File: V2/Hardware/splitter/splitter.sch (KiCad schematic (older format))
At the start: 21 parts, among them J0 Rpi_40Pin_F, J1 Control_seg:1, J2 Control_seg:2, J3 Control_seg:3, J4 Molex_PSU_F, J5 Siren, J6 USB_A_F, K0 RELRAS0515, Q1 BD139-16

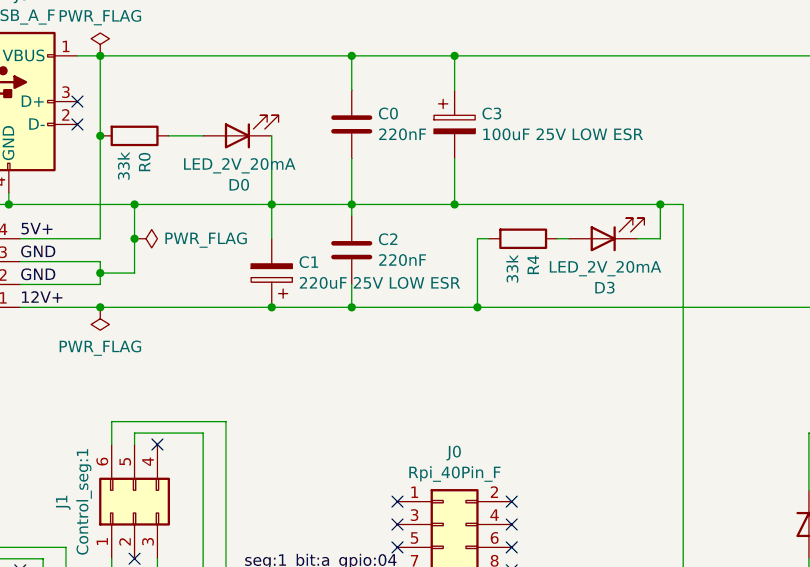
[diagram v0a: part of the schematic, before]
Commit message: update capacitors
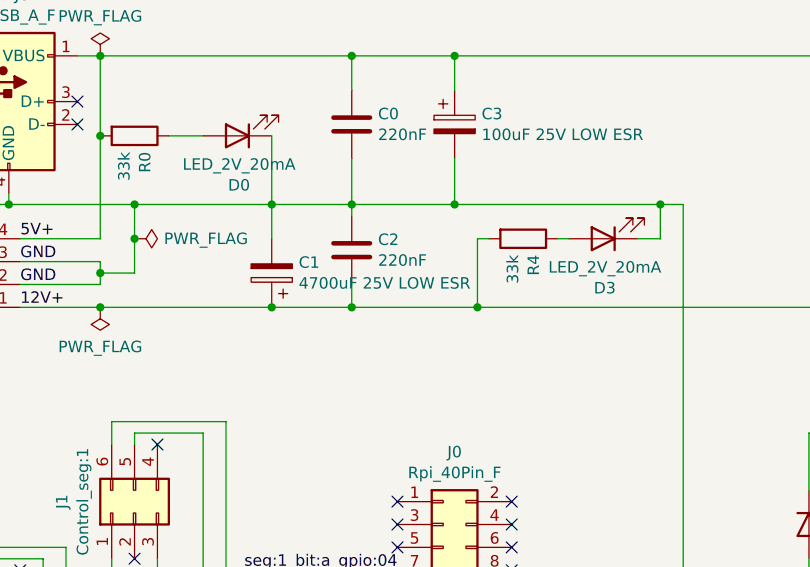
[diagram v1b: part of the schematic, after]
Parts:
- C1: value 220uF 25V LOW ESR -> 4700uF 25V LOW ESR; footprint Capacitor_THT:CP_Radial_D8.0mm_P3.50mm -> Capacitor_THT:CP_Radial_D18.0mm_P7.50mm
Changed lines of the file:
@@
 P 5050 2700
 F 0 "C1" H 4932 2654 50  0000 R CNN
-F 1 "220uF 25V LOW ESR" H 4932 2745 50  0000 R CNN
-F 2 "Capacitor_THT:CP_Radial_D8.0mm_P3.50mm" H 5088 2550 50  0001 C CNN
+F 1 "4700uF 25V LOW ESR" H 4932 2745 50  0000 R CNN
+F 2 "Capacitor_THT:CP_Radial_D18.0mm_P7.50mm" H 5088 2550 50  0001 C CNN
 F 3 "~" H 5050 2700 50  0001 C CNN
 	1    5050 2700

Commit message: Update files
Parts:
- C1: value 4700uF 25V LOW ESR -> 220uF 25V LOW ESR; footprint Capacitor_THT:CP_Radial_D18.0mm_P7.50mm -> Capacitor_THT:CP_Radial_D8.0mm_P3.50mm
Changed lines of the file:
@@
 P 5050 2700
 F 0 "C1" H 4932 2654 50  0000 R CNN
-F 1 "4700uF 25V LOW ESR" H 4932 2745 50  0000 R CNN
-F 2 "Capacitor_THT:CP_Radial_D18.0mm_P7.50mm" H 5088 2550 50  0001 C CNN
+F 1 "220uF 25V LOW ESR" H 4932 2745 50  0000 R CNN
+F 2 "Capacitor_THT:CP_Radial_D8.0mm_P3.50mm" H 5088 2550 50  0001 C CNN
 F 3 "~" H 5050 2700 50  0001 C CNN
 	1    5050 2700
